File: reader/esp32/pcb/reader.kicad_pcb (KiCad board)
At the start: 2 copper layers, 68.2 x 31.9 mm, 28 parts, among them J1 Debug, J2 RS485, Q1 MMBT3904, Q2 MMBT3904, U1 ESP32-WROOM-32U, U2 RDM6300, U3 MAX485E, U5 AMS1117-3.3

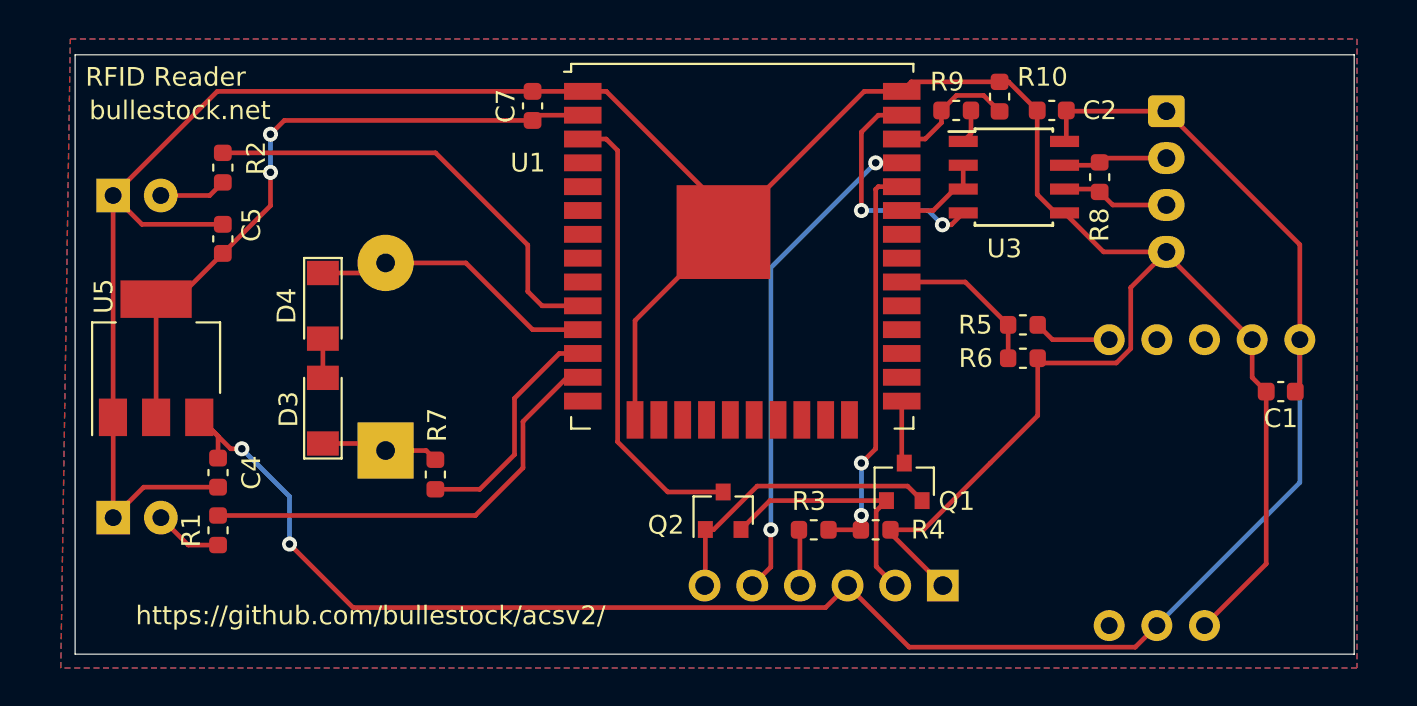
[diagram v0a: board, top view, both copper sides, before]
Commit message: Add RTS pullup; move RS485 connector.
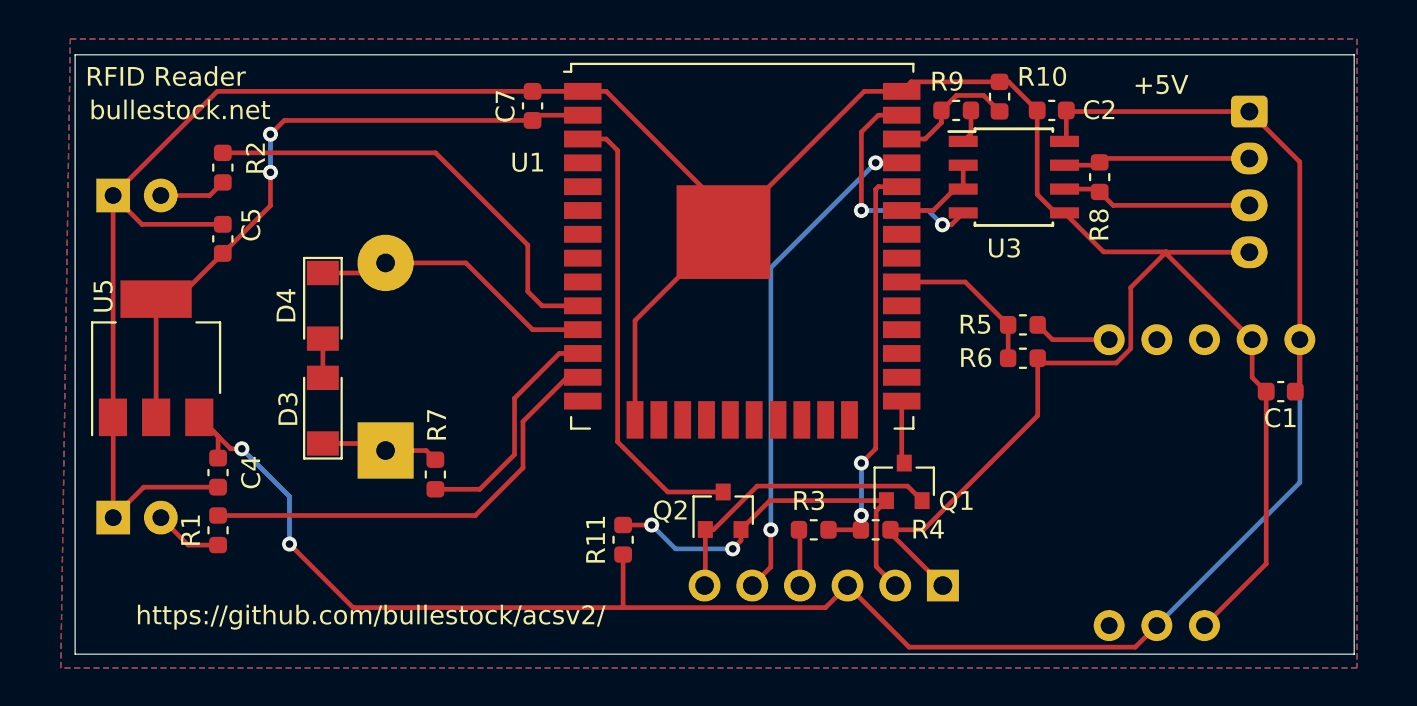
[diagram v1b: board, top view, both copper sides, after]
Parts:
- added R11: 4k7, Resistor_SMD:R_0603_1608Metric, F.Cu at (73.7, 68.4)
- moved J2 4.42 mm to (107.0, 45.5)
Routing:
- net RTS: track 13.6 -> 21.1 mm, vias 0 -> 2
- net +5V: track 105.1 -> 110.5 mm
- net Net-(J2-Pin_2): track 5.59 -> 10.3 mm
- net Net-(J2-Pin_3): track 5.78 -> 10.2 mm
- net GND: track 166.2 -> 170.7 mm
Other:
- board text added: "+5V"

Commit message: Optimize routing.
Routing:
- net +5V: track 110.5 -> 111.5 mm

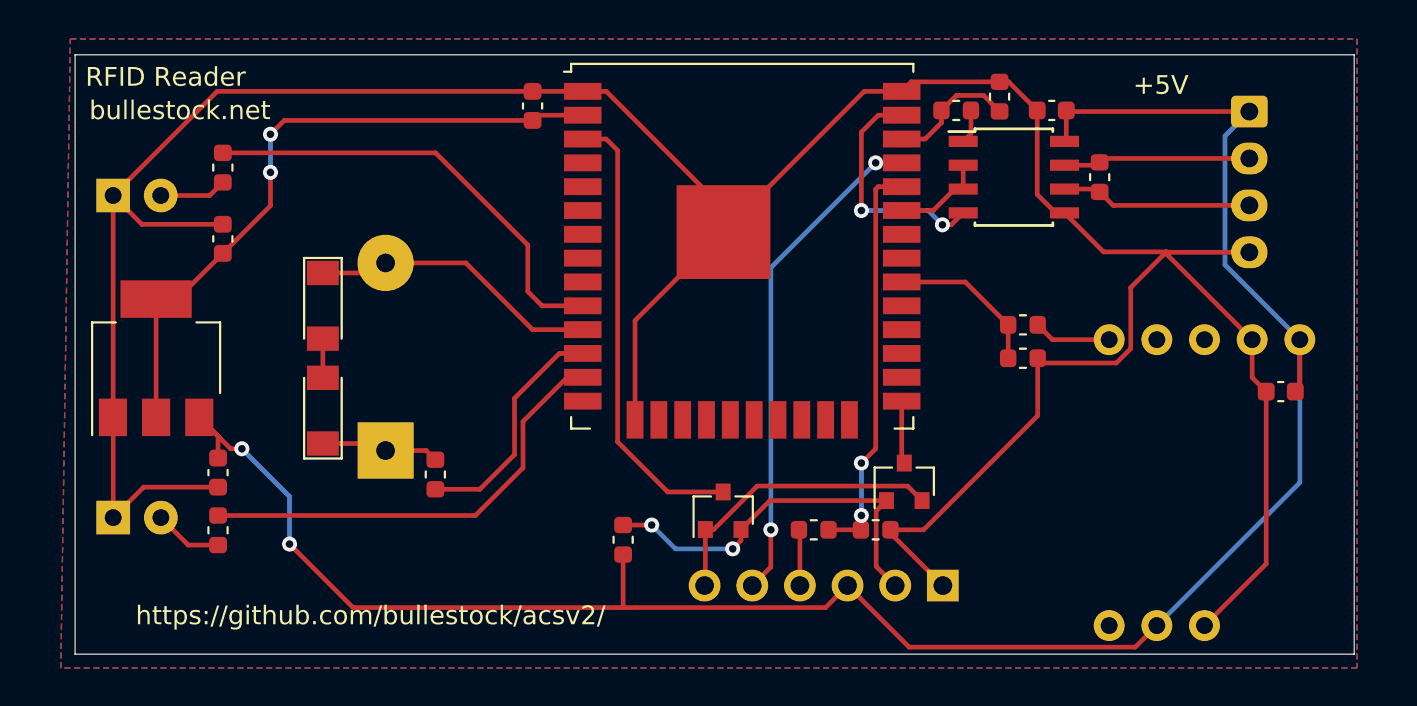
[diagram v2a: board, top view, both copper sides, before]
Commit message: Add reset/boot switches, minimize size.
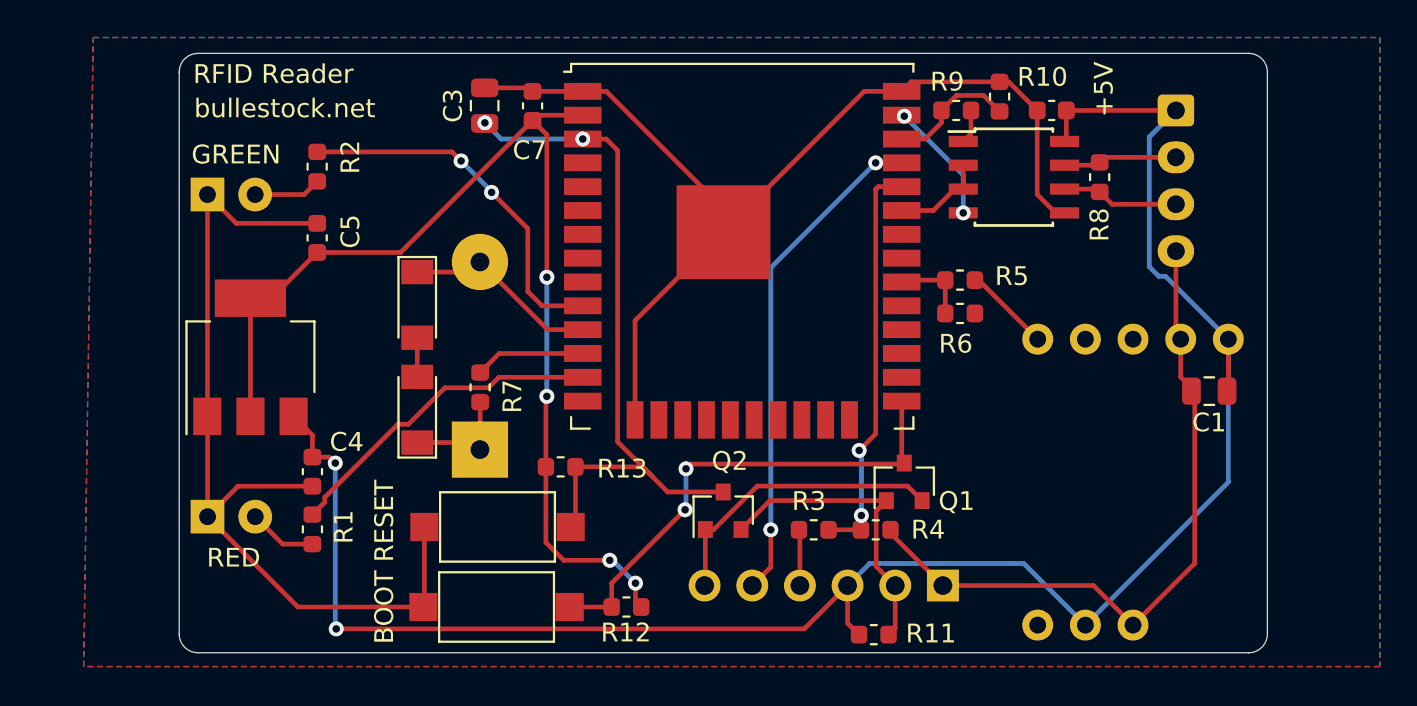
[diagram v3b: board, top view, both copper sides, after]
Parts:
- added C3: 10u, Capacitor_SMD:C_0805_2012Metric, F.Cu at (66.3, 45.2)
- added R12: 10k, Resistor_SMD:R_0603_1608Metric, F.Cu at (73.8, 71.9)
- added R13: 10k, Resistor_SMD:R_0603_1608Metric, F.Cu at (70.3, 64.5)
- added SW1: SW_SPST, Button_Switch_SMD:SW_SPST_CK_RS282G05A3, F.Cu at (67.0, 67.7)
- added SW2: SW_SPST, Button_Switch_SMD:SW_SPST_CK_RS282G05A3, F.Cu at (66.9, 71.9)
- C1: footprint Capacitor_SMD:C_0603_1608Metric -> Capacitor_SMD:C_0805_2012Metric
- moved R11 14.3 mm to (87.0, 73.4), turned to 0 degrees
- moved R7 5.23 mm to (66.0, 60.2), turned to -90 degrees
- moved BZ1 5.03 mm to (66.0, 58.5)
- moved C4 5.03 mm to (57.1, 64.7)
- moved C5 5.03 mm to (57.4, 52.3)
- moved D1 5.03 mm to (51.5, 67.1)
- moved D2 5.03 mm to (51.5, 49.9)
- moved R1 5.03 mm to (57.1, 67.8)
- moved R2 5.03 mm to (57.4, 48.5)
- moved D3 5.03 mm to (62.7, 61.4)
- moved D4 5.03 mm to (62.7, 55.8)
- moved U5 5.03 mm to (53.8, 58.6)
- moved R5 4.12 mm to (91.6, 54.5)
- moved R6 4.12 mm to (91.6, 56.3)
- moved J2 3.92 mm to (103.1, 45.5)
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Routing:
- net GND: track 170.7 -> 140.5 mm
- net BOOT: track 3.36 -> 26.4 mm, vias 0 -> 2
- net +3V3: track 35.3 -> 58.0 mm, vias 2 -> 4
- net RESET: track 24.4 -> 37.6 mm, vias 0 -> 2
- net +5V: track 111.5 -> 102.0 mm
- net BUZ1: track 12.6 -> 5.89 mm
- net RED: track 23.9 -> 17.6 mm
- net TX485: track 12.7 -> 6.61 mm
- net BUZ2: track 15.5 -> 10.5 mm
- net RTS: track 21.1 -> 16.3 mm, vias 2 -> 0
- net GREEN: track 24.0 -> 19.5 mm, vias 0 -> 2
- net ESP_RFID_TX: track 8.40 -> 4.14 mm
- net Net-(J2-Pin_2): track 10.3 -> 6.11 mm
- net Net-(J2-Pin_3): track 10.2 -> 6.27 mm
- net Net-(U2-TX): track 4.14 -> 4.66 mm
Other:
- board size 68.2 x 31.9 mm -> 58 x 31.9 mm
- board text added: "BOOT"
- board text added: "GREEN"
- board text added: "RED"
- board text added: "RESET"

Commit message: Make corners round.
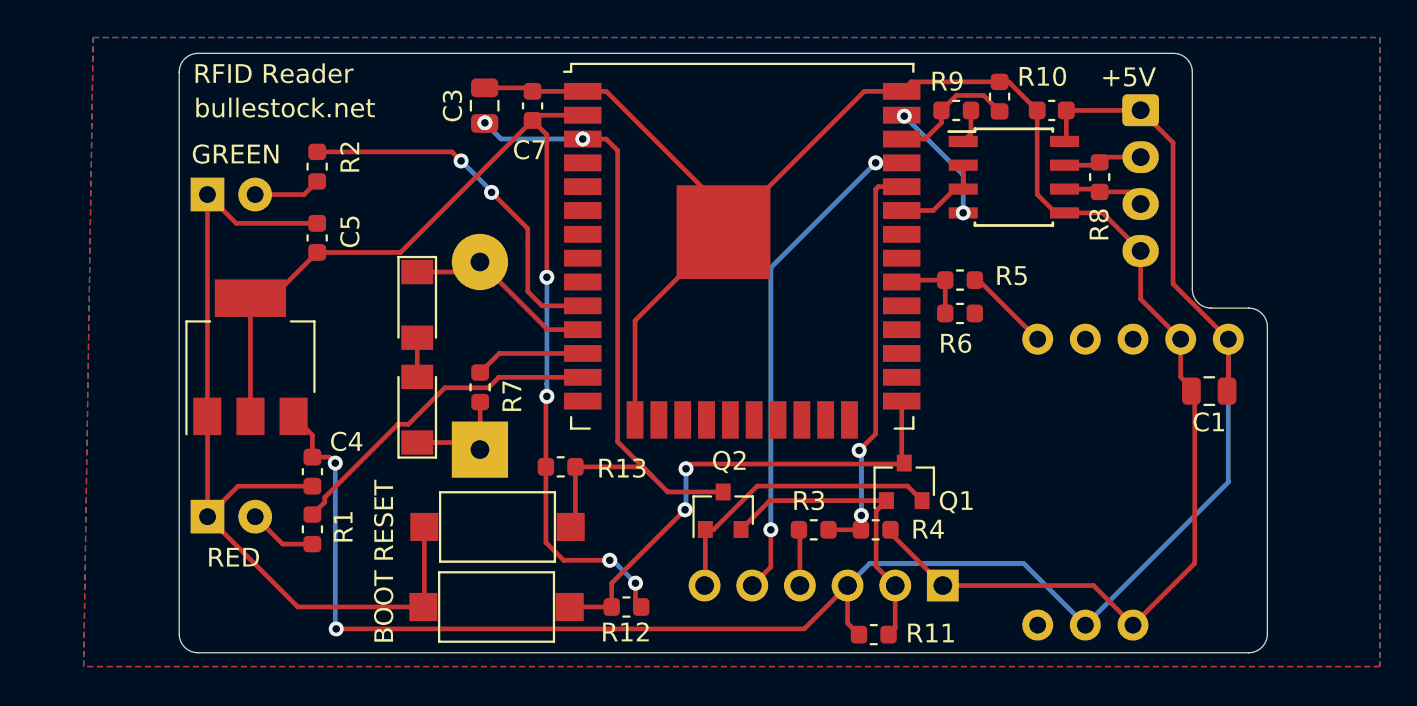
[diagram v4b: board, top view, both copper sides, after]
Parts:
- moved J2 1.88 mm to (101.2, 45.5)
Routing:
- net GND: track 140.5 -> 146.2 mm
- net +5V: track 102.0 -> 99.5 mm
- net Net-(J2-Pin_3): track 6.27 -> 4.39 mm
- net Net-(J2-Pin_2): track 6.11 -> 4.24 mm
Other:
- outline, holes or cut-outs redrawn
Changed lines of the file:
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@@
 		(tags "resistor")
 		(property "Reference" "R11"
-			(at 3.048 -0.0508 360)
+			(at 3.048 -0.0508 0)
 			(layer "F.SilkS")
 			(effects
@@
 		)
 		(property "Value" "4k7"
-			(at 0 1.43 360)
+			(at 0 1.43 0)
 			(layer "F.Fab")
 			(hide yes)
@@
 		)
 		(fp_text user "${REFERENCE}"
-			(at 0 0 360)
+			(at 0 0 0)
 			(layer "F.Fab")
 			(effects
@@
 	(footprint "Connector_JST:JST_XH_S04B-XH-A_1x04_P2.50mm_Horizontal"
 		(layer "B.Cu")
-		(at 103.124 45.466 -90)
+		(at 101.2444 45.4552 -90)
 		(descr "JST XH series connector, S04B-XH-A (http://www.jst-mfg.com/product/pdf/eng/eXH.pdf), generated with kicad-footprint-generator")
 		(tags "connector JST XH top entry")
@@
 	)
 	(gr_arc
+		(start 107 56)
+		(mid 107.707106 56.292893)
+		(end 108 57)
+		(stroke
+			(width 0.05)
+			(type default)
+		)
+		(layer "Edge.Cuts")
+	)
+	(gr_arc
+		(start 105 56)
+		(mid 104.292893 55.707107)
+		(end 104 55)
+		(stroke
+			(width 0.05)
+			(type default)
+		)
+		(layer "Edge.Cuts")
+	)
+	(gr_line
+		(start 105 56)
+		(end 107 56)
+		(stroke
+			(width 0.05)
+			(type default)
+		)
+		(layer "Edge.Cuts")
+	)
+	(gr_arc
 		(start 51 74.3712)
 		(mid 50.292893 74.078307)
@@
 	)
 	(gr_line
-		(start 108 43.4238)
+		(start 108 57)
 		(end 108 73.3712)
 		(stroke
@@
 	)
 	(gr_line
+		(start 104 43.4238)
+		(end 104 55)
+		(stroke
+			(width 0.05)
+			(type default)
+		)
+		(layer "Edge.Cuts")
+	)
+	(gr_line
 		(start 50 43.4238)
 		(end 50 73.3712)
@@
 	)
 	(gr_line
-		(start 107 42.4238)
+		(start 103 42.4238)
 		(end 51 42.4238)
 		(stroke
@@
 	)
 	(gr_arc
-		(start 107 42.4238)
-		(mid 107.707107 42.716693)
-		(end 108 43.4238)
+		(start 103 42.4238)
+		(mid 103.707107 42.716693)
+		(end 104 43.4238)
 		(stroke
 			(width 0.05)
@@
 	)
 	(gr_text "+5V"
-		(at 99.8728 45.8216 90)
+		(at 99.1108 44.2976 0)
 		(layer "F.SilkS")
 		(effects
@@
 	)
 	(segment
-		(start 58.3692 73.1012)
-		(end 83.312 73.1012)
+		(start 102.9716 54.7116)
+		(end 102.9716 47.1824)
 		(width 0.25)
 		(layer "F.Cu")
@@
 	)
 	(segment
-		(start 83.312 73.1012)
-		(end 85.6234 70.7898)
+		(start 58.3692 73.1012)
+		(end 83.312 73.1012)
 		(width 0.25)
 		(layer "F.Cu")
@@
 	)
 	(segment
-		(start 103.124 45.466)
-		(end 97.282 45.466)
+		(start 83.312 73.1012)
+		(end 85.6234 70.7898)
 		(width 0.25)
 		(layer "F.Cu")
@@
 	)
 	(segment
+		(start 105.918 57.658)
+		(end 102.9716 54.7116)
+		(width 0.25)
+		(layer "F.Cu")
+		(net 3)
+	)
+	(segment
 		(start 97.282 45.466)
 		(end 97.282 47.023)
@@
 	)
 	(segment
+		(start 101.2336 45.466)
+		(end 101.2444 45.4552)
+		(width 0.25)
+		(layer "F.Cu")
+		(net 3)
+	)
+	(segment
 		(start 58.0006 63.9442)
 		(end 58.3184 64.262)
@@
 	)
 	(segment
+		(start 97.282 45.466)
+		(end 101.2336 45.466)
+		(width 0.25)
+		(layer "F.Cu")
+		(net 3)
+	)
+	(segment
 		(start 85.6234 72.7965)
 		(end 86.2329 73.406)
@@
 	)
 	(segment
+		(start 102.9716 47.1824)
+		(end 101.2444 45.4552)
+		(width 0.25)
+		(layer "F.Cu")
+		(net 3)
+	)
+	(segment
 		(start 97.342 45.526)
 		(end 97.282 45.466)
@@
 	)
 	(segment
-		(start 102.5652 54.3052)
-		(end 105.918 57.658)
-		(width 0.25)
-		(layer "B.Cu")
-		(net 3)
-	)
-	(segment
-		(start 101.7016 53.7972)
-		(end 102.2096 54.3052)
-		(width 0.25)
-		(layer "B.Cu")
-		(net 3)
-	)
-	(segment
-		(start 103.124 45.466)
-		(end 101.7016 46.8884)
-		(width 0.25)
-		(layer "B.Cu")
-		(net 3)
-	)
-	(segment
 		(start 86.7984 69.6148)
 		(end 95.0148 69.6148)
@@
 	)
 	(segment
-		(start 102.2096 54.3052)
-		(end 102.5652 54.3052)
-		(width 0.25)
-		(layer "B.Cu")
-		(net 3)
-	)
-	(segment
 		(start 95.0148 69.6148)
 		(end 98.298 72.898)
@@
 	)
 	(segment
-		(start 101.7016 46.8884)
-		(end 101.7016 53.7972)
-		(width 0.25)
-		(layer "B.Cu")
-		(net 3)
-	)
-	(segment
 		(start 105.918 57.658)
 		(end 105.918 65.278)
@@
 	)
 	(segment
+		(start 97.188 50.927)
+		(end 99.2162 50.927)
+		(width 0.25)
+		(layer "F.Cu")
+		(net 4)
+	)
+	(segment
 		(start 88.51 44.45)
 		(end 86.51 44.45)
@@
 	)
 	(segment
+		(start 101.2444 52.9552)
+		(end 101.2444 55.5244)
+		(width 0.25)
+		(layer "F.Cu")
+		(net 4)
+	)
+	(segment
 		(start 71.51 44.45)
 		(end 72.76 44.45)
@@
 	)
 	(segment
-		(start 103.124 57.404)
+		(start 101.2444 55.5244)
 		(end 103.378 57.658)
 		(width 0.25)
@@
 	)
 	(segment
-		(start 103.378 57.658)
-		(end 103.378 59.6776)
+		(start 99.2162 50.927)
+		(end 101.2444 52.9552)
 		(width 0.25)
 		(layer "F.Cu")
@@
 	)
 	(segment
-		(start 103.124 52.966)
-		(end 103.124 57.404)
+		(start 103.378 57.658)
+		(end 103.378 59.6776)
 		(width 0.25)
 		(layer "F.Cu")
@@
 	)
 	(segment
-		(start 99.3285 47.966)
-		(end 99.06 48.2345)
+		(start 101.2444 47.9552)
+		(end 99.3393 47.9552)
 		(width 0.25)
 		(layer "F.Cu")
@@
 	)
 	(segment
-		(start 103.124 47.966)
-		(end 99.3285 47.966)
+		(start 98.9075 48.387)
+		(end 99.06 48.2345)
 		(width 0.25)
 		(layer "F.Cu")
@@
 	)
 	(segment
-		(start 98.9075 48.387)
+		(start 99.3393 47.9552)
 		(end 99.06 48.2345)
 		(width 0.25)
@@
 	)
 	(segment
-		(start 99.7165 50.466)
+		(start 98.9075 49.657)
 		(end 99.06 49.8095)
 		(width 0.25)
@@
 	)
 	(segment
-		(start 98.9075 49.657)
-		(end 99.06 49.8095)
+		(start 99.06 49.8095)
+		(end 100.5987 49.8095)
 		(width 0.25)
 		(layer "F.Cu")
@@
 	)
 	(segment
-		(start 103.124 50.466)
-		(end 99.7165 50.466)
+		(start 100.5987 49.8095)
+		(end 101.2444 50.4552)
 		(width 0.25)
 		(layer "F.Cu")

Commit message: Fix outline.
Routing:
- net GND: track 146.2 -> 176.9 mm
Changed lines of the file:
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@@
+	)
+	(segment
+		(start 66.281 44.262)
+		(end 57.1934 44.262)
+		(width 0.25)
+		(layer "F.Cu")
+		(net 4)
 	)
 	(segment
@@
 	)
 	(segment
+		(start 101.6508 59.3852)
+		(end 103.378 57.658)
+		(width 0.25)
+		(layer "F.Cu")
+		(net 4)
+	)
+	(segment
 		(start 97.188 50.927)
 		(end 99.2162 50.927)
@@
 	)
 	(segment
+		(start 94.5896 59.3852)
+		(end 101.6508 59.3852)
+		(width 0.25)
+		(layer "F.Cu")
+		(net 4)
+	)
+	(segment
 		(start 53.1362 65.4942)
 		(end 51.5112 67.1192)
@@
 	)
 	(segment
+		(start 57.1934 44.262)
+		(end 51.5062 49.9492)
+		(width 0.25)
+		(layer "F.Cu")
+		(net 4)
+	)
+	(segment
+		(start 92.4052 56.2864)
+		(end 92.4052 57.2008)
+		(width 0.25)
+		(layer "F.Cu")
+		(net 4)
+	)
+	(segment
 		(start 74.295 56.665)
 		(end 79.01 51.95)
@@
 		(start 99.2162 50.927)
 		(end 101.2444 52.9552)
+		(width 0.25)
+		(layer "F.Cu")
+		(net 4)
+	)
+	(segment
+		(start 92.4052 57.2008)
+		(end 94.5896 59.3852)
 		(width 0.25)
 		(layer "F.Cu")
@@
 		(polygon
 			(pts
-				(xy 45.4152 41.5798) (xy 113.9952 41.5798) (xy 113.9952 75.1078) (xy 44.9072 75.1078)
+				(xy 50.7492 43.2816) (xy 69.2912 43.3324) (xy 69.342 72.6948) (xy 50.7492 72.6948)
 			)
 		)
+	)
+	(zone
+		(net 4)
+		(net_name "GND")
+		(layers "F&B.Cu")
+		(hatch edge 0.5)
+		(priority 1)
+		(connect_pads
+			(clearance 0.508)
+		)
+		(min_thickness 0.25)
+		(filled_areas_thickness no)
+		(fill yes
+			(thermal_gap 0.5)
+			(thermal_bridge_width 0.5)
+		)
+		(polygon
+			(pts
+				(xy 102.3112 43.2816) (xy 102.3112 56.9976) (xy 106.6292 56.9976) (xy 106.6292 73.3552) (xy 90.0684 73.3552)
+				(xy 90.0176 43.2816) (xy 90.17 43.2816)
+			)
+		)
